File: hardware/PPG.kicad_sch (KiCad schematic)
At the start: 9 parts

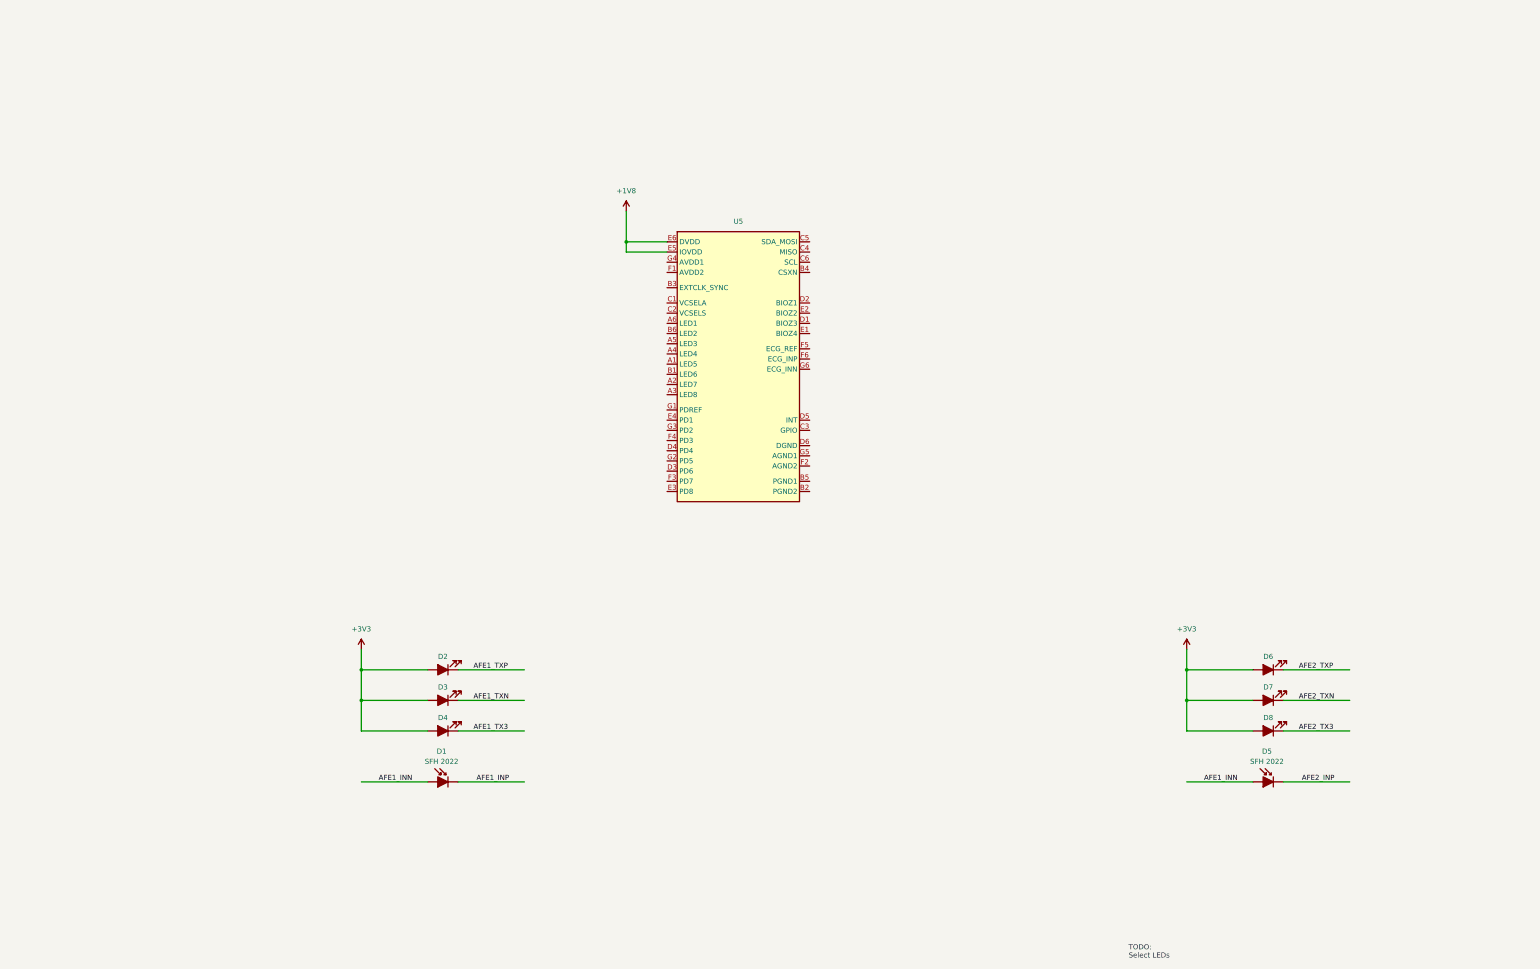
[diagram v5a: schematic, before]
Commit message: Added optical front end submodule and reconnected to STM32
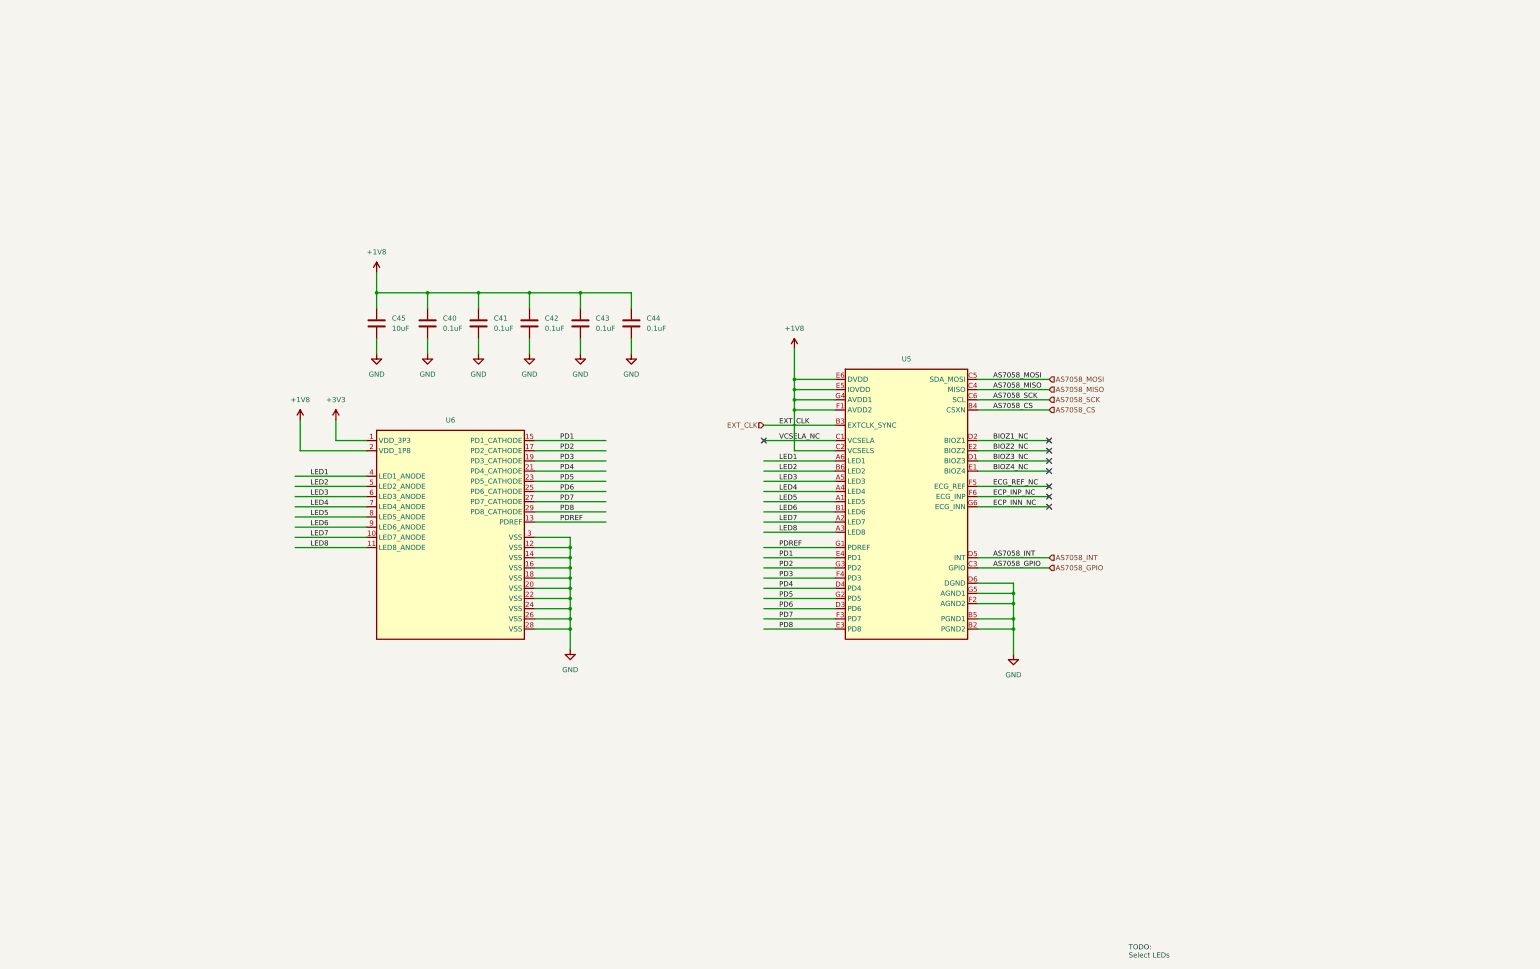
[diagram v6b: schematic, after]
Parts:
- removed D1, D5: SFH 2022, symbol Device:D_Photo_Filled
- removed D2, D3, D4, D6, D7, D8: LED_Filled, symbol Device:LED_Filled
- added C40, C41, C42, C43, C44: 0.1uF, symbol Device:C
- added C45: 10uF, symbol Device:C
- added U6: (no value), symbol Interface:Optical_Front_End
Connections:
- net +1V8: now also U5.C2 (VCSELS), U5.F1 (AVDD2), U5.G4 (AVDD1), C40.1, C41.1, C42.1, C43.1, C44.1, C45.1, U6.2 (VDD_1P8)
- net +3V3: now also U6.1 (VDD_3P3)
- net LED5: now reaches U5.A1 (LED5)
- net LED5: now also U6.8 (LED5_ANODE)
- net LED7: now reaches U5.A2 (LED7)
- net LED7: now also U6.10 (LED7_ANODE)
- net LED8: now reaches U5.A3 (LED8)
- net LED8: now also U6.11 (LED8_ANODE)
- net LED4: now reaches U5.A4 (LED4)
- net LED4: now also U6.7 (LED4_ANODE)
- net LED3: now reaches U5.A5 (LED3)
- net LED3: now also U6.6 (LED3_ANODE)
- net LED1: now reaches U5.A6 (LED1)
- net LED1: now also U6.4 (LED1_ANODE)
- net LED6: now reaches U5.B1 (LED6)
- net LED6: now also U6.9 (LED6_ANODE)
- net GND: now reaches U5.B2 (PGND2)
- net GND: now also U5.B5 (PGND1), U5.D6 (DGND), U5.F2 (AGND2), U5.G5 (AGND1), C40.2, C41.2, C42.2, C43.2, C44.2, C45.2, U6.12 (VSS), U6.14 (VSS), U6.16 (VSS), U6.18 (VSS), U6.20 (VSS), U6.22 (VSS), U6.24 (VSS), U6.26 (VSS), U6.28 (VSS), U6.3 (VSS)
- net EXT_CLK: now reaches U5.B3 (EXTCLK_SYNC)
- net AS7058_CS: now reaches U5.B4 (CSXN)
- net LED2: now reaches U5.B6 (LED2)
- net LED2: now also U6.5 (LED2_ANODE)
- net VCSELA_NC: now reaches U5.C1 (VCSELA)
- net AS7058_GPIO: now reaches U5.C3 (GPIO)
- net AS7058_MISO: now reaches U5.C4 (MISO)
- net AS7058_MOSI: now reaches U5.C5 (SDA_MOSI)
- net AS7058_SCK: now reaches U5.C6 (SCL)
- net BIOZ3_NC: now reaches U5.D1 (BIOZ3)
- net BIOZ1_NC: now reaches U5.D2 (BIOZ1)
- net PD6: now reaches U5.D3 (PD6)
- net PD6: now also U6.25 (PD6_CATHODE)
- net PD4: now reaches U5.D4 (PD4)
- net PD4: now also U6.21 (PD4_CATHODE)
- net AS7058_INT: now reaches U5.D5 (INT)
- net BIOZ4_NC: now reaches U5.E1 (BIOZ4)
- net BIOZ2_NC: now reaches U5.E2 (BIOZ2)
- net PD8: now reaches U5.E3 (PD8)
- net PD8: now also U6.29 (PD8_CATHODE)
- net PD1: now reaches U5.E4 (PD1)
- net PD1: now also U6.15 (PD1_CATHODE)
- net PD7: now reaches U5.F3 (PD7)
- net PD7: now also U6.27 (PD7_CATHODE)
- net PD3: now reaches U5.F4 (PD3)
- net PD3: now also U6.19 (PD3_CATHODE)
- net ECG_REF_NC: now reaches U5.F5 (ECG_REF)
- net ECP_INP_NC: now reaches U5.F6 (ECG_INP)
- net PDREF: now reaches U5.G1 (PDREF)
- net PDREF: now also U6.13 (PDREF)
- net PD5: now reaches U5.G2 (PD5)
- net PD5: now also U6.23 (PD5_CATHODE)
- net PD2: now reaches U5.G3 (PD2)
- net PD2: now also U6.17 (PD2_CATHODE)
- net ECP_INN_NC: now reaches U5.G6 (ECG_INN)
- no-connect marks 0 -> 8
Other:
- moved on the sheet: U5
